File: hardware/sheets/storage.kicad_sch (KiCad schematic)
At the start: 19 parts, among them J1 Conn_02x20_Odd_Even, J2 Conn_02x25_Odd_Even, U1 74HCT04, U10 74HCT573, U2 74HCT08, U3 74HCT08, U4 74HCT32, U5 74HCT125, U6 74HCT138, U7 74HCT138, U8 74HCT245, U9 74HCT573

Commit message: Fix all medium design-review findings (M1-M8)
- M1: Supervisor link moved to GPIO4/5 (real UART1 pair); POST -> GPIO6-15
- M2: CNT_RUN = LD0.LD1.LD2 gates every '163 CEP (load-cascade hazard)
- M3: ~WR / IO-M pruned to cpu_core-internal; DRQ2/3 pulled + noted;
  doc S5.2 "as built: 48/48" + S16 updated
- M4: true XT-IDE rev-2 map (A0<->A3 swap): data 0x300, latch 0x301,
  CS1 0x307/0x30F, drive DA0 = bus A3 - matches XTIDE UB "rev 2" type
- M5: COM4 -> bus IRQ2 line (IRQ9 via AT redirect); IRQ10/11/14/15 marked
  off-header; ~REFRESH added to mxbus ISA_CTRL; questions-sidecar superseded
- M6: card_isatest clock tree on unswitched V5RAW (spec S8)
- M7: card_isatest IRQ2-8/DRQ1-3 idle pull-downs (spec S4/S9)
- M8: com_port JP1 selects 16550 RX source (DB9 vs TTL console); 5V note

Rebuilt motherboard + cards; structural ERC = 0; netlist-verified.
Fix log in hardware/notes/design-review-2026-07-03.md (batch 3).

Co-Authored-By: Claude Fable 5 <noreply@anthropic.com>
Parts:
- added U11: 74HCT138, symbol mini-xt:74HCT138
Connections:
- net +5V: now also U11.16 (VCC), U11.6 (E2)
- net A0: now also U6.1 (A0); no longer J1.35 (Pin_35), J2.20 (Pin_20), U7.1 (A0)
- net A1: now also U7.1 (A0), U11.1 (A0); no longer U7.2 (A1)
- net A2: now also U7.2 (A1), U11.2 (A1); no longer U7.3 (A2)
- net A3: now also J1.35 (Pin_35), J2.20 (Pin_20), U7.3 (A2), U11.3 (A2); no longer U6.1 (A0)
- net GND: now also U11.5 (~{E1}), U11.8 (GND)
- net ~{DATA_SEL}: now also U11.15 (~{Y0}); no longer U7.15 (~{Y0})
- net ~{HB_SEL}: now also U7.15 (~{Y0}); no longer U6.13 (~{Y2})
- net ~{IDE_CS0}: now also U11.4 (~{E0}); no longer U7.4 (~{E0})
- net ~{IDE_CS1}: now also U3.6 (P6); no longer U6.14 (~{Y1})
- net ~{CS1_A}: now reaches U3.4 (P4)
- net ~{CS1_A}: now also U7.12 (~{Y3})
- net ~{CS1_B}: now reaches U3.5 (P5)
- net ~{CS1_B}: now also U7.7 (~{Y7})
- new net ~{ODD_SEL}: U6.14 (~{Y1}), U7.4 (~{E0})
- no-connect marks 40 -> 44

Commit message: JLCPCB sourcing pass: verify pinouts, LCSC part numbers, SMD build
Custom-symbol verification (open-questions Q5 resolved):
- MAX3241 symbol was wrong on nearly every pin and used MAX3243-style
  control names; regenerated to the real SSOP-28 pinout (SHDN#/EN#/
  R1OUTB/R2OUTB) and com_port rewired -- EN# must be GROUNDED (the old
  ~FORCEON-high would have disabled the receivers on real silicon)
- DS12C887 symbol wrong on 4 pins (DS=17, RESET#=18, IRQ#=19, SQW=23)

Sourcing (every part checked against the JLC DB; ~45 line items):
- New tools/parts.py maps (lib_id, value) -> LCSC; build.py applies it as
  an 'LCSC Part Num' property on every component (384 across the project)
- Sheets stay generic; stock-forced substitutions bound in the map:
  '374->'574 (parallel rewired), '163->'161, '157->HC157 (+HCT-buffered
  3.3V selects, I0/I1 swapped), '02->HC02, TCM809->MCP809, 2N3904->MMBT3904
- bus_mcu address counters moved to the 3.3V domain (HC161 on 3V3_BUS,
  loaded from MCU-side MD0-7; HCT244s read the 3.3V outputs at TTL Vih)
- 14.318 XOs are 3.3V-only parts: powered from 3V3, squared up via spare
  HCT gates (cpu_core U13, card_isatest U19)
- COM baud reference is now a 1.8432MHz crystal on the 16C550's XIN/XOUT
  (3.3V-only oscillators vs a 5V-only soft card)
- Supervisor QSPI header replaced with a real W25Q128JVSIQ
- Socket policy (fab installs sockets): V20 DIP-40, SRAM DIP-32 (no 5V
  512Kx8 SRAM at JLC at all), DS12C887 DIP-24, female headers for modules

Docs: CLAUDE.md fabrication-constraints section (SMD, 100x100mm, generic-
symbols rule, voltage-domain rule); README + hardware/README fab notes;
notes/jlcpcb-sourcing.md (decisions, thin-stock flags, not-at-JLC list);
stale questions-sidecar.md collapsed to its supersession record.

Rebuilt motherboard + cards: structural ERC 0, byte-identical rebuilds.

Co-Authored-By: Claude Fable 5 <noreply@anthropic.com>
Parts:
- C1, C2, C3, C4: LCSC Part Num (none) -> C14663
- J1: LCSC Part Num (none) -> C2333
- J2: LCSC Part Num (none) -> C2962036
- R1, R2, R3: LCSC Part Num (none) -> C25804
- U1: LCSC Part Num (none) -> C672096
- U10, U9: LCSC Part Num (none) -> C5209384
- U11, U6, U7: LCSC Part Num (none) -> C5965
- U2, U3: LCSC Part Num (none) -> C5959
- U4: LCSC Part Num (none) -> C5985
- U5: LCSC Part Num (none) -> C5962
- U8: LCSC Part Num (none) -> C5979
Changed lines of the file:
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@@
+			)
+		)
+		(property "LCSC Part Num" "C672096"
+			(at 38.1 76.2 0)
+			(effects
+				(font
+					(size 1.27 1.27)
+				)
+				(hide yes)
 			)
 		)
@@
 			)
 		)
+		(property "LCSC Part Num" "C5959"
+			(at 38.1 142.24 0)
+			(effects
+				(font
+					(size 1.27 1.27)
+				)
+				(hide yes)
+			)
+		)
 		(pin "1"
 		)
@@
 			)
 		)
+		(property "LCSC Part Num" "C5959"
+			(at 38.1 205.74 0)
+			(effects
+				(font
+					(size 1.27 1.27)
+				)
+				(hide yes)
+			)
+		)
 		(pin "1"
 		)
@@
 			)
 		)
+		(property "LCSC Part Num" "C5985"
+			(at 114.3 210.82 0)
+			(effects
+				(font
+					(size 1.27 1.27)
+				)
+				(hide yes)
+			)
+		)
 		(pin "1"
 		)
@@
 			)
 		)
+		(property "LCSC Part Num" "C5962"
+			(at 38.1 256.54 0)
+			(effects
+				(font
+					(size 1.27 1.27)
+				)
+				(hide yes)
+			)
+		)
 		(pin "2"
 		)
@@
 			)
 		)
+		(property "LCSC Part Num" "C5965"
+			(at 114.3 63.5 0)
+			(effects
+				(font
+					(size 1.27 1.27)
+				)
+				(hide yes)
+			)
+		)
 		(pin "1"
 		)
@@
 			)
 		)
+		(property "LCSC Part Num" "C5965"
+			(at 114.3 142.24 0)
+			(effects
+				(font
+					(size 1.27 1.27)
+				)
+				(hide yes)
+			)
+		)
 		(pin "1"
 		)
@@
 			)
 		)
+		(property "LCSC Part Num" "C5965"
+			(at 152.4 63.5 0)
+			(effects
+				(font
+					(size 1.27 1.27)
+				)
+				(hide yes)
+			)
+		)
 		(pin "1"
 		)
@@
 			)
 		)
+		(property "LCSC Part Num" "C5979"
+			(at 190.5 63.5 0)
+			(effects
+				(font
+					(size 1.27 1.27)
+				)
+				(hide yes)
+			)
+		)
 		(pin "1"
 		)
@@
 			)
 		)
+		(property "LCSC Part Num" "C5209384"
+			(at 190.5 142.24 0)
+			(effects
+				(font
+					(size 1.27 1.27)
+				)
+				(hide yes)
+			)
+		)
 		(pin "2"
 		)
@@
 			)
 		)
+		(property "LCSC Part Num" "C5209384"
+			(at 190.5 215.9 0)
+			(effects
+				(font
+					(size 1.27 1.27)
+				)
+				(hide yes)
+			)
+		)
 		(pin "2"
 		)
@@
 			)
 		)
+		(property "LCSC Part Num" "C2333"
+			(at 292.1 127 0)
+			(effects
+				(font
+					(size 1.27 1.27)
+				)
+				(hide yes)
+			)
+		)
 		(pin "1"
 		)
@@
 			)
 		)
+		(property "LCSC Part Num" "C2962036"
+			(at 368.3 127 0)
+			(effects
+				(font
+					(size 1.27 1.27)
+				)
+				(hide yes)
+			)
+		)
 		(pin "1"
 		)
@@
 			)
 		)
+		(property "LCSC Part Num" "C25804"
+			(at 228.6 25.4 0)
+			(effects
+				(font
+					(size 1.27 1.27)
+				)
+				(hide yes)
+			)
+		)
 		(pin "1"
 		)
@@
 			)
 		)
+		(property "LCSC Part Num" "C25804"
+			(at 243.84 25.4 0)
+			(effects
+				(font
+					(size 1.27 1.27)
+				)
+				(hide yes)
+			)
+		)
 		(pin "1"
 		)
@@
 			)
 		)
+		(property "LCSC Part Num" "C25804"
+			(at 259.08 25.4 0)
+			(effects
+				(font
+					(size 1.27 1.27)
+				)
+				(hide yes)
+			)
+		)
 		(pin "1"
 		)
@@
 			)
 		)
+		(property "LCSC Part Num" "C14663"
+			(at 49.53 276.86 0)
+			(effects
+				(font
+					(size 1.27 1.27)
+				)
+				(hide yes)
+			)
+		)
 		(pin "1"
 		)
@@
 			)
 		)
+		(property "LCSC Part Num" "C14663"
+			(at 100.33 276.86 0)
+			(effects
+				(font
+					(size 1.27 1.27)
+				)
+				(hide yes)
+			)
+		)
 		(pin "1"
 		)
@@
 			)
 		)
+		(property "LCSC Part Num" "C14663"
+			(at 149.86 276.86 0)
+			(effects
+				(font
+					(size 1.27 1.27)
+				)
+				(hide yes)
+			)
+		)
 		(pin "1"
 		)
@@
 			(at 199.39 276.86 0)
 			(effects
+				(font
+					(size 1.27 1.27)
+				)
+				(hide yes)
+			)
+		)
+		(property "LCSC Part Num" "C14663"
+			(at 199.39 276.86 0)
+			(effects

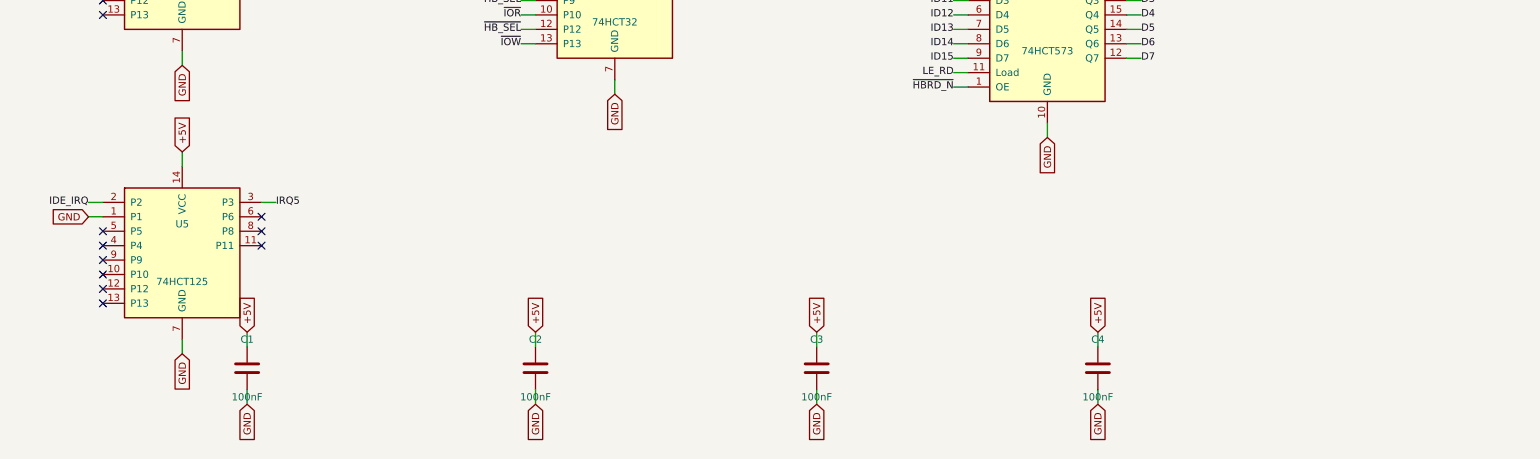
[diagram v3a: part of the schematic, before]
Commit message: Design review 2026-07-11: rail protection, decoupling, wiring fixes
Protection:
- Sidecar +5V now feeds through a 2A polyfuse into +5V_ISA with an
  SMBJ5.0A clamp + 22uF bulk (a faulted ISA card trips its own fuse
  instead of dropping the board; back-fed voltage is clamped).
- USB-C VBUS enters through a 3A polyfuse with an SMBJ5.0A on +5V
  (backstop for the CFG1 9-20V failure mode). CH224K gains a 1uF VDD
  cap; its PG routes to Supervisor GPIO16 as PD_PG. Buck output
  doubled to 2x22uF, 10uF at VIN, extra rail bulk.
- Supervisor USB-A host port: 27R series termination (RP2040
  requirement), USBLC6-2SC6 ESD array, 100uF VBUS bulk.
- Video: HDMI +5V fused (500mA), HPD sensed on GPIO41, 100R series on
  VGA sync. TMDS ESD array deferred to layout (no symbol).
- card_isatest: V5RAW bulk, Q1 gate soft-start cap, TVS on DUT rail.

Wiring fixes:
- SPKR had no driver anywhere (netlist: 1 node). Bus MCU GPIO22
  reassigned from the diagnostics-only bus-CLK sense to SPKR; bus_mcu
  drops CLK from its interface. Doc 5.2 updated.
- bus_mcu C8 decoupled +3V3, a rail that sheet never uses -> 3V3_BUS.
- Storage IRQ5 was push-pull (permanently driven when idle) -> 2N7002
  + gated '125 tri-state, same convention as the LPT IRQ7 stage.
- MAX3241 pump caps resized to the 5V datasheet values (47nF/330nF).
- LPT DB25 status inputs get 4.7k pull-ups (floated with no printer).
- Audio line-out gets a 100R series isolator before the jack.

Best practices:
- Decoupling to ~1x100nF per IC on every sheet + bulk per board
  (cpu_core 7->16 incl. the naked 3.3V oscillator, storage 4->11,
  parallel 6->13, rtc/com/video/bus_mcu/card_isatest similar).
- All floating spare CMOS inputs tied ('00/'74/'157/'02/'04/'125
  sections across cpu_core, bus_mcu, rtc, storage, card_isatest).

Sourcing: new parts mapped in parts.py with JLC-verified LCSC numbers;
Power_Protection lib registered in the tools; TPS563200 stock alert
(4 pcs left at JLC) flagged in parts.py + jlcpcb-sourcing.md. All
decisi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
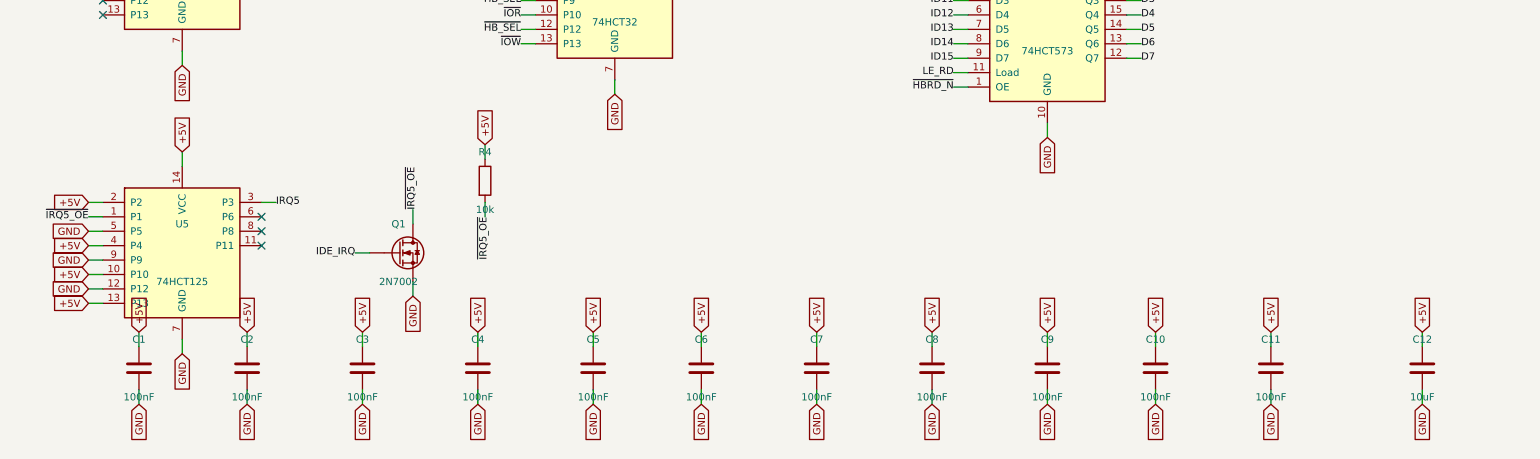
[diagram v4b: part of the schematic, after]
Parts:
- added C10, C11, C5, C6, C7, C8, C9: 100nF, symbol Device:C
- added C12: 10uF, symbol Device:C
- added Q1: 2N7002, symbol Device:Q_NMOS
- added R4: 10k, symbol Device:R
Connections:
- net +5V: now also U5.10 (P10), U5.13 (P13), U5.2 (P2), U5.4 (P4), C10.1, C11.1, C12.1, C5.1, C6.1, C7.1, C8.1, C9.1, R4.1
- net GND: now also U5.12 (P12), U5.5 (P5), U5.9 (P9), C10.2, C11.2, C12.2, C5.2, C6.2, C7.2, C8.2, C9.2, Q1.S; no longer U5.1 (P1)
- net IDE_IRQ: now also Q1.G; no longer U5.2 (P2)
- new net ~{IRQ5_OE}: Q1.D, R4.2, U5.1 (P1)
- no-connect marks 44 -> 38

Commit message: Storage/video: enable + base-address straps
Completes the jumper story started with COM/LPT: every on-board peripheral
can now be disabled or re-strapped to make room for the same card on the
sidecar chain.

- storage: JP1 base 0x300/0x320 (differ only in A5; A5_SEL replaces nA5 in
  the HI_MATCH tree, XTIDE UB supports both) and JP2 enable on DEC1's spare
  ~E1 (open kills /CS0 + /ODD_SEL, so DEC2/DEC3, both high-byte latches and
  the low-byte '245 go inert; INTRQ's pull-down keeps IRQ5 released). Same
  pattern as the LPT sheet.
- video: firmware-read boot straps -- this snoop card decodes in firmware,
  so there is no hardware chip-select to gate. JP1/VID_EN (GPIO42, 10k to
  3V3_VID) open = firmware keeps every bus-facing OE off (all drivers are
  MCU-gated tri-states, so a disabled card is electrically silent);
  JP2/VID_BASE (GPIO43) closed = CGA windows (0x3D4/0xB8000), open =
  MDA/Hercules (0x3B4/0xB0000) -- the snoop equivalent of a period card's
  MDA/CGA switch.

Design doc updated (8, 10, 14 I/O map); decisions logged in
questions-storage.md / questions-video.md.

Verified: motherboard + cards rebuild with zero structural ERC; netlist
ties each strap to its jumper, pull resistor and decode/GPIO pin
(A5_SEL/~{STOR_EN} on storage, VID_EN/VID_BASE on the video module).

Co-Authored-By: Claude Fable 5 <noreply@anthropic.com>
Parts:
- added C1: 100nF, symbol Device:C
- added JP2: STOR_EN, symbol Connector_Generic:Conn_01x02
- added R5: 10k, symbol Device:R
- JP1: renamed from C1; value 100nF -> BASE 300/320; symbol Device:C -> Connector_Generic:Conn_01x03; LCSC Part Num C14663 -> C2337
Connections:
- net +5V: now also C1.1, R5.1; no longer JP1.1
- net A5: now also JP1.3 (Pin_3)
- net GND: now also C1.2, JP2.2 (Pin_2); no longer JP1.2, U6.5 (~{E1})
- net nA5: now also JP1.1 (Pin_1); no longer U2.4 (P4)
- new net A5_SEL: JP1.2 (Pin_2), U2.4 (P4)
- new net ~{STOR_EN}: JP2.1 (Pin_1), R5.2, U6.5 (~{E1})
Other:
- note added: "JP1 base 0x300/0x320 (XTIDE UB supports both); JP2 open = card disabled."

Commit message: Storage: on-board only, IRQ14-default strap; 16-bit IRQ collector
Remove card_storage (same rationale as COM/LPT/RTC -- the on-board sheet
carries the full jumper set; ~25-line wrapper, restorable from git).
Standalone PCBs remaining: video + the isatest jig.

- storage: JP3 IRQ strap -- 1-2 = IRQ14 (DEFAULT, the AT primary-IDE
  convention), 2-3 = IRQ5 (XT fallback; also the LPT alternate), open =
  polled. The '125 now drives STOR_IRQ into the strap, so the unselected
  line is untouched.
- bus_mcu: IRQ14 had no physical path into the soft-PIC, so the IRQ
  collector is now a cascaded pair of 74HCT165s (U19 IRQ10-15 -> U12
  IRQ2-9, net IRQ_CAS), with R19-R24 idle pull-downs and C18. Zero GPIO
  cost -- same IRQ_LOAD/IRQ_CLK/IRQ_SER, firmware shifts 16 bits. Also
  un-dangles the IRQ10-15 interface pins the sheet had declared since day
  one. IRQ10-15 are motherboard-internal (the 60-pin header carries only
  IRQ2-8).
- README: XT-IDE moves into the on-board peripherals list (all three
  straps + the shadow-loaded-BIOS note); motherboard is the third board;
  coexistence example now pairs the on-board XT-IDE with a real ISA IDE
  card at 0x320.
- Design doc: 4.3 card list, 10 JP3 strap + XTIDE UB IRQ-config note
  (was still "Poll or IRQ5"), 5.2 collector row, 14 IRQ table (IRQ14 no
  longer "spare"), 15 BOM row. Decisions logged in open-questions.md,
  questions-storage.md, questions-bus_mcu.md.

Verified: motherboard + both cards rebuild with zero structural ERC;
netlist shows /IRQ14 = {JP3, pull-down, U19 collector input} spanning
storage<->bus_mcu, IRQ_CAS = U19.Q7 -> U12.DS, and /IRQ5 still carrying
sidecar + LPT strap + collector.

Co-Authored-By: Claude Fable 5 <noreply@anthropic.com>
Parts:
- added JP3: IRQ 14/5, symbol Connector_Generic:Conn_01x03
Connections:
- net IRQ5: now also JP3.3 (Pin_3); no longer U5.3 (P3)
- new net IRQ14: JP3.1 (Pin_1)
- new net STOR_IRQ: JP3.2 (Pin_2), U5.3 (P3)
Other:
- note added: "JP1 base 0x300/0x320 (XTIDE UB); JP2 open = card disabled; JP3 1-2=IRQ14(default)/2-3=IRQ5/open=polled."
- note removed: "JP1 base 0x300/0x320 (XTIDE UB supports both); JP2 open = card disabled."
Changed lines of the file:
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@@
 		)
 	)
+	(hierarchical_label "IRQ14"
+		(shape output)
+		(at 25.4 83.82 0)
+		(effects
+			(font
+				(size 1.27 1.27)
+			)
+		)
+	)
 	(wire
 		(pts
@@
 		)
 	)
-	(label "IRQ5"
+	(label "STOR_IRQ"
 		(at 54.61 247.65 0)
 		(effects
@@
 	(wire
 		(pts
+			(xy 299.72 22.86)
+			(xy 302.26 22.86)
+		)
+		(stroke
+			(width 0)
+			(type default)
+		)
+	)
+	(label "IRQ14"
+		(at 302.26 22.86 0)
+		(effects
+			(font
+				(size 1.27 1.27)
+			)
+		)
+	)
+	(wire
+		(pts
+			(xy 299.72 25.4)
+			(xy 302.26 25.4)
+		)
+		(stroke
+			(width 0)
+			(type default)
+		)
+	)
+	(label "STOR_IRQ"
+		(at 302.26 25.4 0)
+		(effects
+			(font
+				(size 1.27 1.27)
+			)
+		)
+	)
+	(wire
+		(pts
+			(xy 299.72 27.94)
+			(xy 302.26 27.94)
+		)
+		(stroke
+			(width 0)
+			(type default)
+		)
+	)
+	(label "IRQ5"
+		(at 302.26 27.94 0)
+		(effects
+			(font
+				(size 1.27 1.27)
+			)
+		)
+	)
+	(wire
+		(pts
 			(xy 320.04 21.59)
 			(xy 320.04 19.05)
@@
 		)
 	)
-	(text "JP1 base 0x300/0x320 (XTIDE UB supports both); JP2 open = card disabled."
+	(text "JP1 base 0x300/0x320 (XTIDE UB); JP2 open = card disabled; JP3 1-2=IRQ14(default)/2-3=IRQ5/open=polled."
 		(at 266.7 17.78 0)
 		(effects
@@
 					(unit 1)
 				)
+			)
+		)
+	)
+	(symbol
+		(lib_id "Connector_Generic:Conn_01x03")
+		(at 304.8 25.4 0)
+		(unit 1)
+		(exclude_from_sim no)
+		(in_bom yes)
+		(on_board yes)
+		(dnp no)
+		(fields_autoplaced yes)
+		(property "Reference" "JP3"
+			(at 304.8 20.32 0)
+			(effects
+				(font
+					(size 1.27 1.27)
+				)
+			)
+		)
+		(property "Value" "IRQ 14/5"
+			(at 304.8 30.48 0)
+			(effects
+				(font
+					(size 1.27 1.27)
+				)
+			)
+		)
+		(property "Footprint" ""
+			(at 304.8 25.4 0)
+			(effects
+				(font
+					(size 1.27 1.27)
+				)
+				(hide yes)
+			)
+		)
+		(property "LCSC Part Num" "C2337"
+			(at 304.8 25.4 0)
+			(effects
+				(font
+					(size 1.27 1.27)
+				)
+				(hide yes)
+			)
+		)
+		(pin "1"
+		)
+		(pin "2"
+		)
+		(pin "3"
+		)
+		(instances
+			(project "mini-xt"
+				(path "/26736c46-8b40-5460-874f-03596d17270c/934dc409-a4cb-59b8-b7c0-94f3033c354b"
+					(reference "JP1003")
+					(unit 1)
+				)
